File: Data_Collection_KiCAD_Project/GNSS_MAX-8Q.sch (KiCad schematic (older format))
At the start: 13 parts, among them J4 Conn_Coaxial, Q1 FDC6330L, U4 MAX-8Q

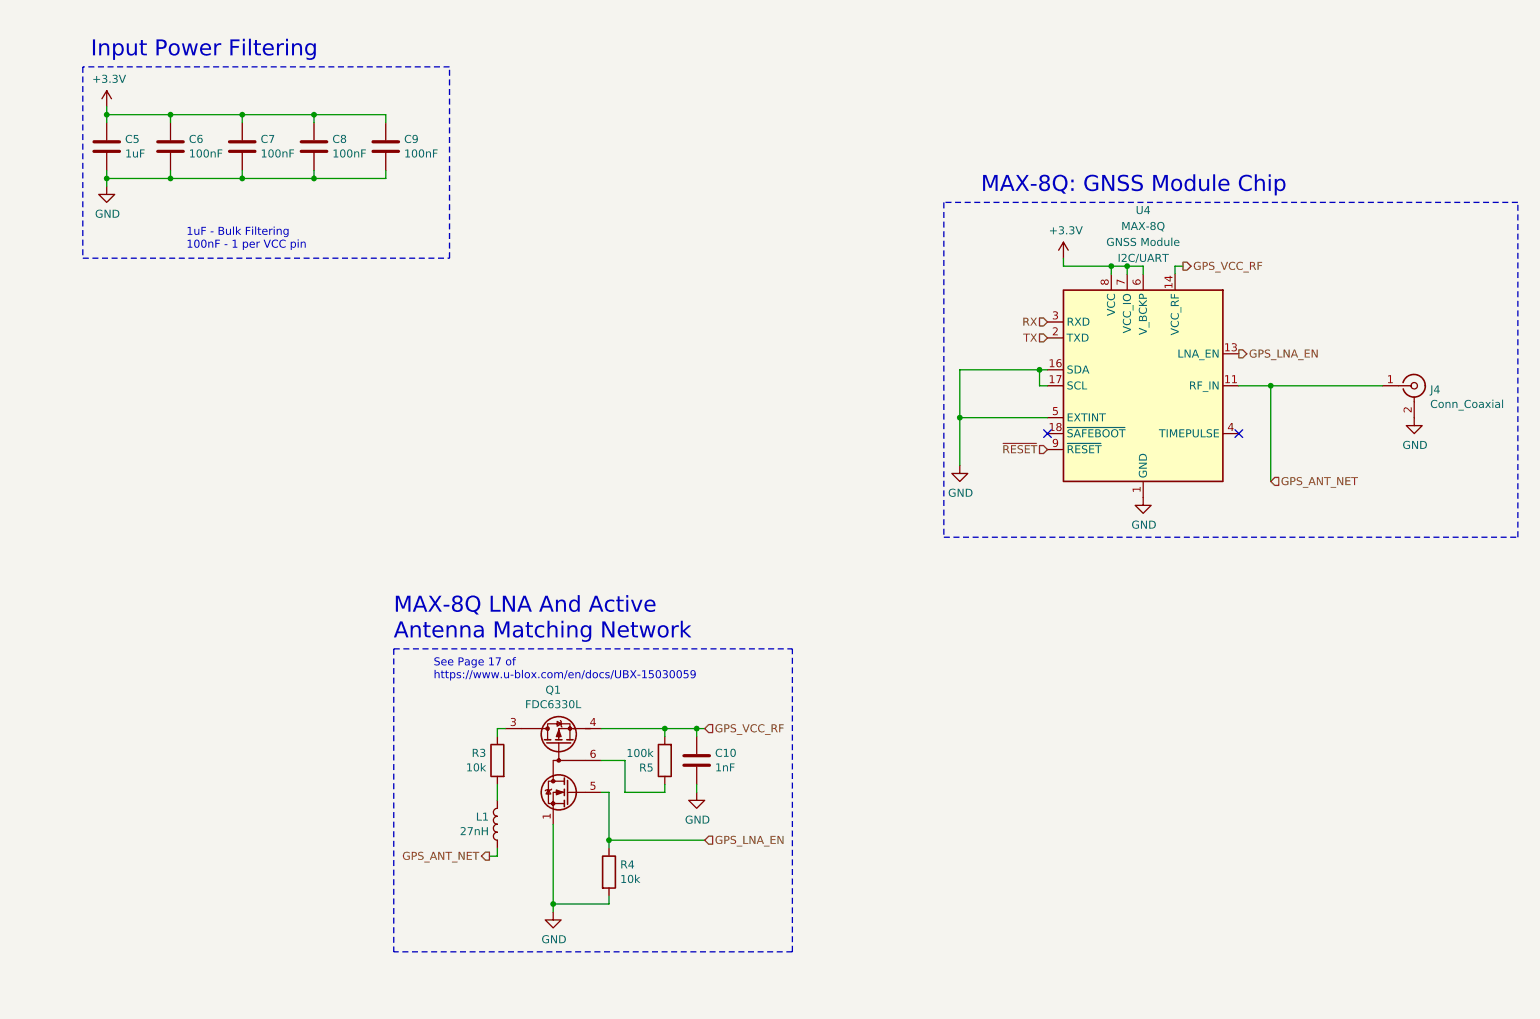
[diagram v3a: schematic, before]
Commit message: footprint changes
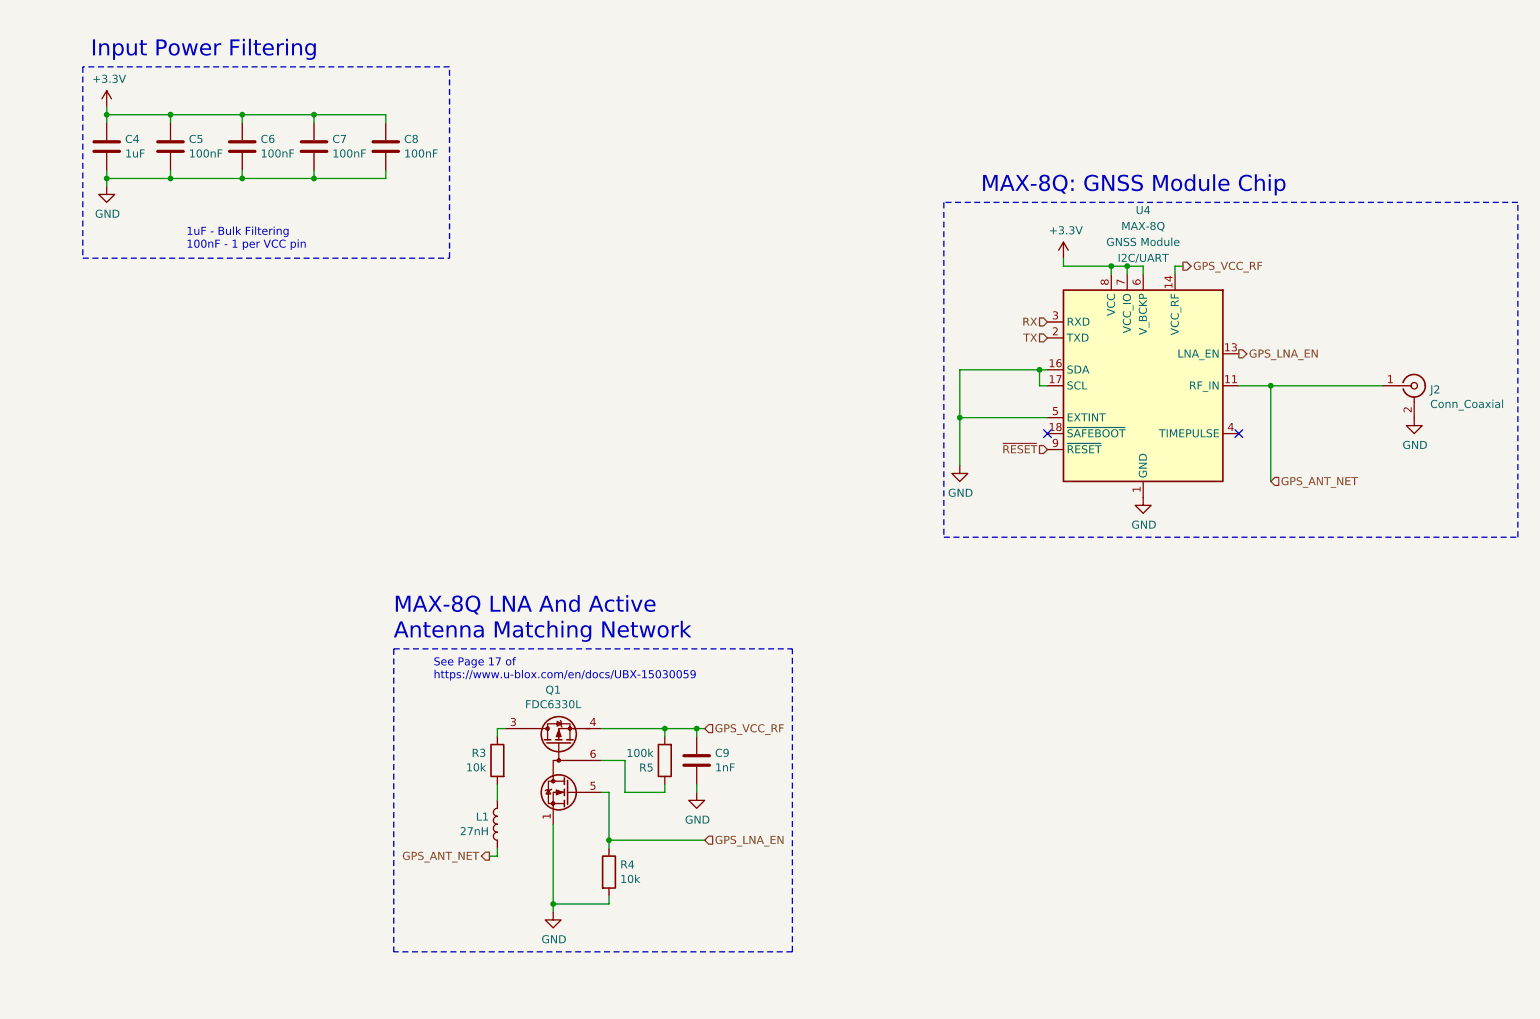
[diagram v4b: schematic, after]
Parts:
- renumbered C5 to C4, C6 to C5, C7 to C6, C8 to C7, C9 to C8, C10 to C9, J4 to J2
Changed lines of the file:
@@
 P 4000 6500
 AR Path="/616192D6" Ref="#PWR?"  Part="1"
-AR Path="/615A5F2C/616192D6" Ref="#PWR025"  Part="1"
-F 0 "#PWR025" H 4000 6250 50  0001 C CNN
+AR Path="/615A5F2C/616192D6" Ref="#PWR018"  Part="1"
+F 0 "#PWR018" H 4000 6250 50  0001 C CNN
 F 1 "GND" H 4005 6327 50  0000 C CNN
 F 2 "" H 4000 6500 50  0001 C CNN
@@
 P 4900 5550
 AR Path="/616192DC" Ref="C?"  Part="1"
-AR Path="/615A5F2C/616192DC" Ref="C10"  Part="1"
-F 0 "C10" H 5015 5596 50  0000 L CNN
+AR Path="/615A5F2C/616192DC" Ref="C9"  Part="1"
+F 0 "C9" H 5015 5596 50  0000 L CNN
 F 1 "1nF" H 5015 5505 50  0000 L CNN
 F 2 "Capacitor_SMD:C_0603_1608Metric" H 4938 5400 50  0001 C CNN
@@
 P 4900 5750
 AR Path="/616192FE" Ref="#PWR?"  Part="1"
-AR Path="/615A5F2C/616192FE" Ref="#PWR026"  Part="1"
-F 0 "#PWR026" H 4900 5500 50  0001 C CNN
+AR Path="/615A5F2C/616192FE" Ref="#PWR019"  Part="1"
+F 0 "#PWR019" H 4900 5500 50  0001 C CNN
 F 1 "GND" H 4905 5577 50  0000 C CNN
 F 2 "" H 4900 5750 50  0001 C CNN
@@
 P 7200 2400
 AR Path="/6161C95B" Ref="#PWR?"  Part="1"
-AR Path="/615A5F2C/6161C95B" Ref="#PWR028"  Part="1"
-F 0 "#PWR028" H 7200 2250 50  0001 C CNN
+AR Path="/615A5F2C/6161C95B" Ref="#PWR021"  Part="1"
+F 0 "#PWR021" H 7200 2250 50  0001 C CNN
 F 1 "+3.3V" H 7215 2573 50  0000 C CNN
 F 2 "" H 7200 2400 50  0001 C CNN
@@
 P 7700 3900
 AR Path="/6161C967" Ref="#PWR?"  Part="1"
-AR Path="/615A5F2C/6161C967" Ref="#PWR029"  Part="1"
-F 0 "#PWR029" H 7700 3650 50  0001 C CNN
+AR Path="/615A5F2C/6161C967" Ref="#PWR022"  Part="1"
+F 0 "#PWR022" H 7700 3650 50  0001 C CNN
 F 1 "GND" H 7705 3727 50  0000 C CNN
 F 2 "" H 7700 3900 50  0001 C CNN
@@
 P 9400 3200
 AR Path="/6161C976" Ref="J?"  Part="1"
-AR Path="/615A5F2C/6161C976" Ref="J4"  Part="1"
-F 0 "J4" H 9500 3175 50  0000 L CNN
+AR Path="/615A5F2C/6161C976" Ref="J2"  Part="1"
+F 0 "J2" H 9500 3175 50  0000 L CNN
 F 1 "Conn_Coaxial" H 9500 3084 50  0000 L CNN
 F 2 "" H 9400 3200 50  0001 C CNN
@@
 P 1200 1950
 AR Path="/6161C998" Ref="#PWR?"  Part="1"
-AR Path="/615A5F2C/6161C998" Ref="#PWR024"  Part="1"
-F 0 "#PWR024" H 1200 1700 50  0001 C CNN
+AR Path="/615A5F2C/6161C998" Ref="#PWR017"  Part="1"
+F 0 "#PWR017" H 1200 1700 50  0001 C CNN
 F 1 "GND" H 1205 1777 50  0000 C CNN
 F 2 "" H 1200 1950 50  0001 C CNN
@@
 P 1200 1700
 AR Path="/6161C99E" Ref="C?"  Part="1"
-AR Path="/615A5F2C/6161C99E" Ref="C5"  Part="1"
-F 0 "C5" H 1315 1746 50  0000 L CNN
+AR Path="/615A5F2C/6161C99E" Ref="C4"  Part="1"
+F 0 "C4" H 1315 1746 50  0000 L CNN
 F 1 "1uF" H 1315 1655 50  0000 L CNN
 F 2 "Capacitor_SMD:C_0603_1608Metric" H 1238 1550 50  0001 C CNN
@@
 P 1200 1450
 AR Path="/6161C9A4" Ref="#PWR?"  Part="1"
-AR Path="/615A5F2C/6161C9A4" Ref="#PWR023"  Part="1"
-F 0 "#PWR023" H 1200 1300 50  0001 C CNN
+AR Path="/615A5F2C/6161C9A4" Ref="#PWR016"  Part="1"
+F 0 "#PWR016" H 1200 1300 50  0001 C CNN
 F 1 "+3.3V" H 1215 1623 50  0000 C CNN
 F 2 "" H 1200 1450 50  0001 C CNN
@@
 P 1600 1700
 AR Path="/6161C9AC" Ref="C?"  Part="1"
-AR Path="/615A5F2C/6161C9AC" Ref="C6"  Part="1"
-F 0 "C6" H 1715 1746 50  0000 L CNN
+AR Path="/615A5F2C/6161C9AC" Ref="C5"  Part="1"
+F 0 "C5" H 1715 1746 50  0000 L CNN
 F 1 "100nF" H 1715 1655 50  0000 L CNN
 F 2 "Capacitor_SMD:C_0603_1608Metric" H 1638 1550 50  0001 C CNN
@@
 P 2050 1700
 AR Path="/6161C9B2" Ref="C?"  Part="1"
-AR Path="/615A5F2C/6161C9B2" Ref="C7"  Part="1"
-F 0 "C7" H 2165 1746 50  0000 L CNN
+AR Path="/615A5F2C/6161C9B2" Ref="C6"  Part="1"
+F 0 "C6" H 2165 1746 50  0000 L CNN
 F 1 "100nF" H 2165 1655 50  0000 L CNN
 F 2 "Capacitor_SMD:C_0603_1608Metric" H 2088 1550 50  0001 C CNN
@@
 P 2500 1700
 AR Path="/6161C9B8" Ref="C?"  Part="1"
-AR Path="/615A5F2C/6161C9B8" Ref="C8"  Part="1"
-F 0 "C8" H 2615 1746 50  0000 L CNN
+AR Path="/615A5F2C/6161C9B8" Ref="C7"  Part="1"
+F 0 "C7" H 2615 1746 50  0000 L CNN
 F 1 "100nF" H 2615 1655 50  0000 L CNN
 F 2 "Capacitor_SMD:C_0603_1608Metric" H 2538 1550 50  0001 C CNN
@@
 P 2950 1700
 AR Path="/6161C9D2" Ref="C?"  Part="1"
-AR Path="/615A5F2C/6161C9D2" Ref="C9"  Part="1"
-F 0 "C9" H 3065 1746 50  0000 L CNN
+AR Path="/615A5F2C/6161C9D2" Ref="C8"  Part="1"
+F 0 "C8" H 3065 1746 50  0000 L CNN
 F 1 "100nF" H 3065 1655 50  0000 L CNN
 F 2 "Capacitor_SMD:C_0603_1608Metric" H 2988 1550 50  0001 C CNN
@@
 P 9400 3400
 AR Path="/61679BC7" Ref="#PWR?"  Part="1"
-AR Path="/615A5F2C/61679BC7" Ref="#PWR030"  Part="1"
-F 0 "#PWR030" H 9400 3150 50  0001 C CNN
+AR Path="/615A5F2C/61679BC7" Ref="#PWR023"  Part="1"
+F 0 "#PWR023" H 9400 3150 50  0001 C CNN
 F 1 "GND" H 9405 3227 50  0000 C CNN
 F 2 "" H 9400 3400 50  0001 C CNN
@@
 P 6550 3700
 AR Path="/6167BBB2" Ref="#PWR?"  Part="1"
-AR Path="/615A5F2C/6167BBB2" Ref="#PWR027"  Part="1"
-F 0 "#PWR027" H 6550 3450 50  0001 C CNN
+AR Path="/615A5F2C/6167BBB2" Ref="#PWR020"  Part="1"
+F 0 "#PWR020" H 6550 3450 50  0001 C CNN
 F 1 "GND" H 6555 3527 50  0000 C CNN
 F 2 "" H 6550 3700 50  0001 C CNN

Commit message: Finalized Schematic
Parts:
- J2: footprint (none) -> Connector_Coaxial:SMA_Amphenol_132134-11_Vertical
- L1: footprint (none) -> Inductor_THT:L_Radial_D10.5mm_P5.00mm_Abacron_AISR-01
- Q1: value FDC6330L -> SI1040X-T1-GE3; footprint Package_TO_SOT_SMD:TSOT-23-6 -> SC-89:SC-89; symbol Data_Collection_KiCAD_Project-rescue:FDC6330L-Transistor_FET-Data_Collection_KiCAD_Project-rescue -> Transistor_FET:FDC6330L
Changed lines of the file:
@@
 $EndDescr
-$Comp
-L Data_Collection_KiCAD_Project-rescue:L-Device-Data_Collection_KiCAD_Project-rescue L?
-U 1 1 616192D0
-P 3650 5950
-AR Path="/616192D0" Ref="L?"  Part="1"
-AR Path="/615A5F2C/616192D0" Ref="L1"  Part="1"
-F 0 "L1" H 3703 5996 50  0000 L CNN
-F 1 "27nH" H 3703 5905 50  0000 L CNN
-F 2 "" H 3650 5950 50  0001 C CNN
-F 3 "~" H 3650 5950 50  0001 C CNN
-	1    3650 5950
-	-1   0    0    -1
-$EndComp
 $Comp
 L Data_Collection_KiCAD_Project-rescue:GND-power-Data_Collection_KiCAD_Project-rescue #PWR?
@@
 	1    0    0    -1
 $EndComp
-$Comp
-L Data_Collection_KiCAD_Project-rescue:FDC6330L-Transistor_FET-Data_Collection_KiCAD_Project-rescue Q?
-U 1 1 616192EF
-P 4000 5650
-AR Path="/616192EF" Ref="Q?"  Part="1"
-AR Path="/615A5F2C/616192EF" Ref="Q1"  Part="1"
-F 0 "Q1" H 4000 6192 50  0000 C CNN
-F 1 "FDC6330L" H 4000 6101 50  0000 C CNN
-F 2 "Package_TO_SOT_SMD:TSOT-23-6" H 3950 5075 50  0001 C CNN
-F 3 "https://www.onsemi.com/pub/Collateral/FDC6330L-D.PDF" H 3900 5550 50  0001 C CNN
-	1    4000 5650
-	-1   0    0    -1
-$EndComp
 Wire Wire Line
 	4700 5400 4700 5350
@@
 	4900 5350 4950 5350
 Connection ~ 4900 5350
-$Comp
-L Data_Collection_KiCAD_Project-rescue:R-Device-Data_Collection_KiCAD_Project-rescue R?
-U 1 1 61619311
-P 3650 5550
-AR Path="/61619311" Ref="R?"  Part="1"
-AR Path="/615A5F2C/61619311" Ref="R3"  Part="1"
-F 0 "R3" H 3720 5596 50  0000 L CNN
-F 1 "10k" H 3720 5505 50  0000 L CNN
-F 2 "Resistor_SMD:R_0603_1608Metric" V 3580 5550 50  0001 C CNN
-F 3 "~" H 3650 5550 50  0001 C CNN
-	1    3650 5550
-	-1   0    0    -1
-$EndComp
 Wire Wire Line
 	4350 6050 4950 6050
-Wire Wire Line
-	3650 5800 3650 5700
-Wire Wire Line
-	3650 6100 3650 6150
-Wire Wire Line
-	3650 6150 3600 6150
 Text Notes 3250 5050 0    50   ~ 0
                   See Page 17 of \nhttps://www.u-blox.com/en/docs/UBX-15030059
 Wire Notes Line
 	5500 6750 5500 4850
-Wire Wire Line
-	3650 5350 3650 5400
-Wire Wire Line
-	3700 5350 3650 5350
-Wire Notes Line
-	3000 4850 3000 6750
 Wire Notes Line
 	3000 4850 5500 4850
@@
 F 0 "J2" H 9500 3175 50  0000 L CNN
 F 1 "Conn_Coaxial" H 9500 3084 50  0000 L CNN
-F 2 "" H 9400 3200 50  0001 C CNN
+F 2 "Connector_Coaxial:SMA_Amphenol_132134-11_Vertical" H 9400 3200 50  0001 C CNN
 F 3 " ~" H 9400 3200 50  0001 C CNN
 	1    9400 3200
@@
 Wire Notes Line
 	3350 1200 1050 1200
-Text HLabel 3600 6150 0    50   Output ~ 0
-GPS_ANT_NET
 Wire Notes Line
 	10050 4150 10050 2050
@@
 Text Notes 3000 4800 0    100  ~ 0
 MAX-8Q LNA And Active\nAntenna Matching Network
+Wire Notes Line
+	3000 4850 3000 6750
+$Comp
+L Data_Collection_KiCAD_Project-rescue:L-Device-Data_Collection_KiCAD_Project-rescue L?
+U 1 1 616192D0
+P 3650 5950
+AR Path="/616192D0" Ref="L?"  Part="1"
+AR Path="/615A5F2C/616192D0" Ref="L1"  Part="1"
+F 0 "L1" H 3703 5996 50  0000 L CNN
+F 1 "27nH" H 3703 5905 50  0000 L CNN
+F 2 "Inductor_THT:L_Radial_D10.5mm_P5.00mm_Abacron_AISR-01" H 3650 5950 50  0001 C CNN
+F 3 "~" H 3650 5950 50  0001 C CNN
+	1    3650 5950
+	-1   0    0    -1
+$EndComp
+$Comp
+L Data_Collection_KiCAD_Project-rescue:R-Device-Data_Collection_KiCAD_Project-rescue R?
+U 1 1 61619311
+P 3650 5550
+AR Path="/61619311" Ref="R?"  Part="1"
+AR Path="/615A5F2C/61619311" Ref="R3"  Part="1"
+F 0 "R3" H 3720 5596 50  0000 L CNN
+F 1 "10k" H 3720 5505 50  0000 L CNN
+F 2 "Resistor_SMD:R_0603_1608Metric" V 3580 5550 50  0001 C CNN
+F 3 "~" H 3650 5550 50  0001 C CNN
+	1    3650 5550
+	-1   0    0    -1
+$EndComp
+Wire Wire Line
+	3650 5800 3650 5700
+Wire Wire Line
+	3650 6100 3650 6150
+Wire Wire Line
+	3650 6150 3600 6150
+Text HLabel 3600 6150 0    50   Output ~ 0
+GPS_ANT_NET
+Wire Wire Line
+	3700 5350 3650 5350
+Wire Wire Line
+	3650 5350 3650 5400
+$Comp
+L Transistor_FET:FDC6330L Q?
+U 1 1 616192EF
+P 4000 5650
+AR Path="/616192EF" Ref="Q?"  Part="1"
+AR Path="/615A5F2C/616192EF" Ref="Q1"  Part="1"
+F 0 "Q1" H 4000 6192 50  0000 C CNN
+F 1 "SI1040X-T1-GE3" H 4000 6101 50  0000 C CNN
+F 2 "SC-89:SC-89" H 3950 5075 50  0001 C CNN
+F 3 "https://www.onsemi.com/pub/Collateral/FDC6330L-D.PDF" H 3900 5550 50  0001 C CNN
+	1    4000 5650
+	-1   0    0    -1
+$EndComp
 $EndSCHEMATC

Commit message: routing update
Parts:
- L1: Digikey (none) -> https://www.digikey.com/en/products/detail/abracon-llc/AIUR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
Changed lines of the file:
@@
 F 2 "Inductor_THT:L_Radial_D10.5mm_P5.00mm_Abacron_AISR-01" H 3650 5950 50  0001 C CNN
 F 3 "~" H 3650 5950 50  0001 C CNN
+F 4 "https://www.digikey.com/en/products/detail/abracon-llc/AIUR-04-273J/2343571" H 3650 5950 50  0001 C CNN "Digikey"
 	1    3650 5950
 	-1   0    0    -1
